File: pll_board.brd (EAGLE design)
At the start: 50 x 50 mm, 86 parts, among them U1 SI5351C, U3 MCP47X6, U4 LD117AS33TR, U5 74AC74D, X0 SMA-142-0711-871/876, X1 SMA-142-0711-871/876, X2 SMA-142-0711-871/876, X3 SMA-142-0711-871/876, X4 SMA-142-0711-871/876, X5 SMA-142-0711-871/876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

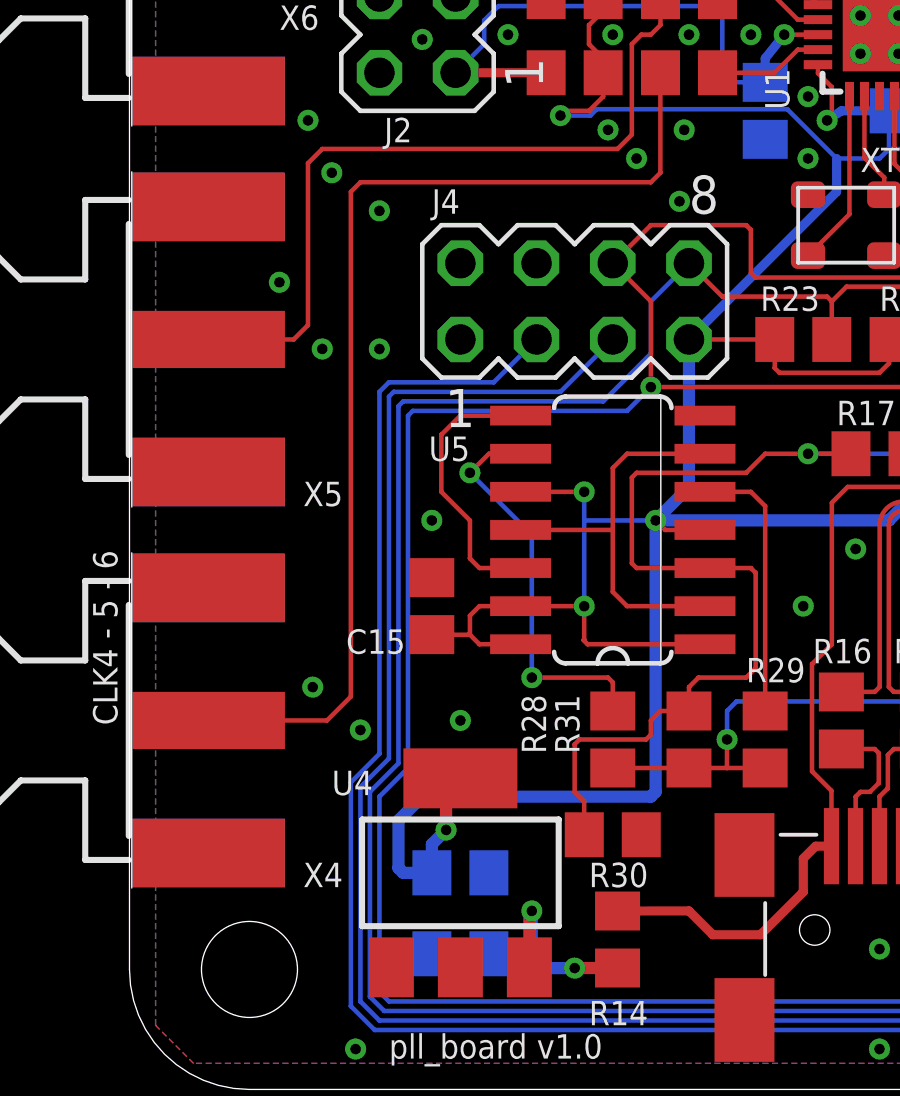
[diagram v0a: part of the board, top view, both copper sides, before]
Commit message: Add USB +5V on i2c/uart connector.
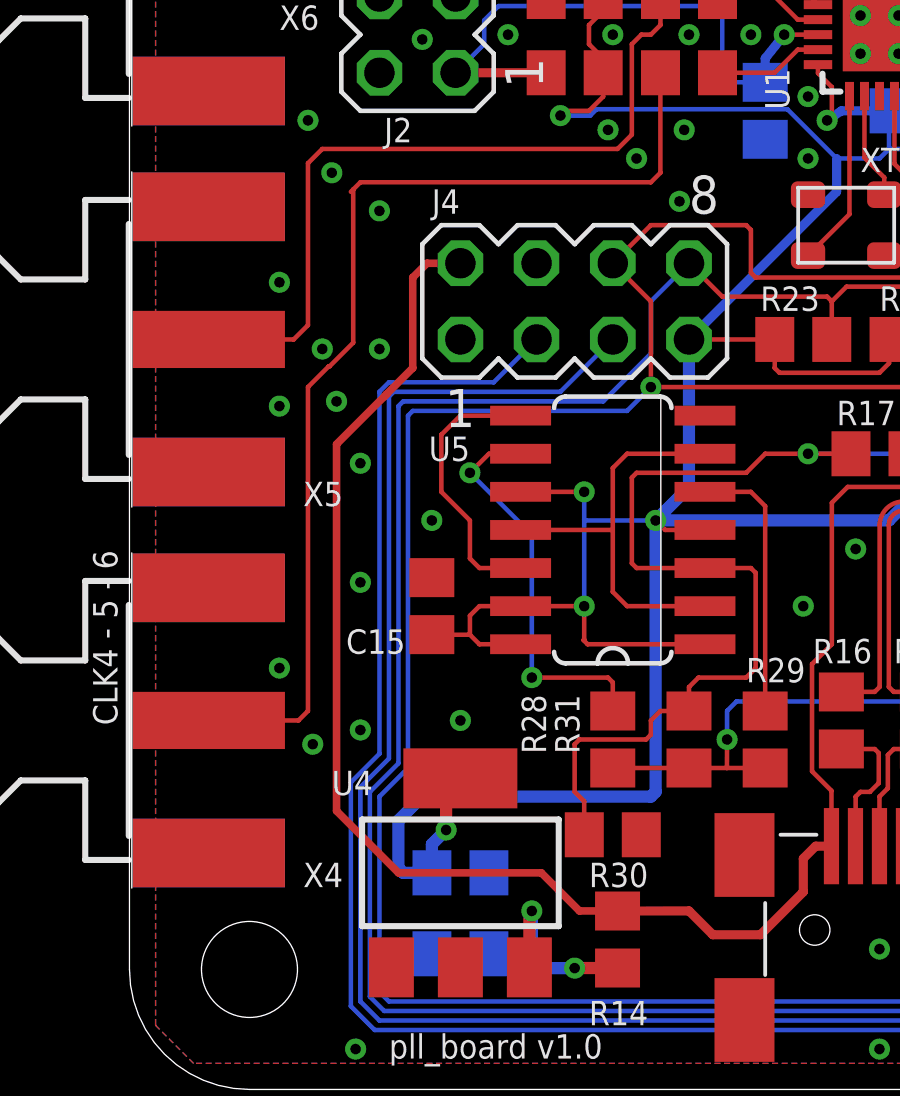
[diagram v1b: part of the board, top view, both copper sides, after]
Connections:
- net +5V: now also J4.2
- net GND: now also J4.4
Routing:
- net +5V: track 33.9 -> 65.4 mm
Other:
- board text added: "Si5351C PLL + ATmega32U4 PLL / OCXO-Control / Clock Generator V1.1 <vogelchr@vogel.cx> http://github.com/vogelchr/pll_board/"
- board text removed: "Si5351C PLL + ATmega32U4 PLL / OCXO-Control / Clock Generator V1.0 <vogelchr@vogel.cx> http://github.com/vogelchr/pll_board/"
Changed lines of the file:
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@@
 <text x="37.94125" y="9.04875" size="0.8128" layer="26" font="vector" rot="MR0">Si5351C PLL + ATmega32U4
 PLL / OCXO-Control / Clock Generator
-V1.0 &lt;vogelchr@vogel.cx&gt;
+V1.1 &lt;vogelchr@vogel.cx&gt;
 http://github.com/vogelchr/pll_board/</text>
 <text x="10.31875" y="2.69875" size="0.8128" layer="25" font="vector">pll_board v1.0</text>
@@
 <via x="17.78" y="36.83" extent="1-16" drill="0.35"/>
 <via x="8.41375" y="32.22625" extent="1-16" drill="0.35"/>
-<via x="7.77875" y="15.08125" extent="1-16" drill="0.35"/>
-<via x="9.36625" y="13.6525" extent="1-16" drill="0.35"/>
+<via x="6.6675" y="15.71625" extent="1-16" drill="0.35"/>
+<via x="7.77875" y="13.17625" extent="1-16" drill="0.35"/>
 <via x="8.09625" y="26.3525" extent="1-16" drill="0.35"/>
 <via x="6.6675" y="28.575" extent="1-16" drill="0.35"/>
@@
 <via x="36.5125" y="23.01875" extent="1-16" drill="0.35"/>
 <via x="28.575" y="20.32" extent="1-16" drill="0.35"/>
+<contactref element="J4" pad="4"/>
+<via x="9.36625" y="13.6525" extent="1-16" drill="0.35"/>
+<via x="9.36625" y="18.57375" extent="1-16" drill="0.35"/>
+<via x="9.36625" y="22.5425" extent="1-16" drill="0.35"/>
 <wire x1="26.035" y1="36.195" x2="26.67" y2="36.83" width="0" layer="19" extent="1-1"/>
+<via x="8.5725" y="24.60625" extent="1-16" drill="0.35"/>
+<via x="6.6675" y="24.4475" extent="1-16" drill="0.35"/>
 </signal>
 <signal name="CLK0_SMA">
@@
 <contactref element="R5" pad="2"/>
 <contactref element="X4" pad="1"/>
-<wire x1="4.31165" y1="13.97" x2="8.255" y2="13.97" width="0.1524" layer="1"/>
-<wire x1="8.255" y1="13.97" x2="9.04875" y2="14.76375" width="0.1524" layer="1"/>
-<wire x1="9.04875" y1="14.76375" x2="9.04875" y2="31.59125" width="0.1524" layer="1"/>
-<wire x1="9.04875" y1="31.59125" x2="9.36625" y2="31.90875" width="0.1524" layer="1"/>
+<wire x1="9.04875" y1="31.59125" x2="9.128125" y2="31.670625" width="0.1524" layer="1"/>
+<wire x1="9.128125" y1="31.670625" x2="9.36625" y2="31.90875" width="0.1524" layer="1"/>
 <wire x1="19.05" y1="31.90875" x2="19.3675" y2="32.22625" width="0.1524" layer="1"/>
 <wire x1="19.3675" y1="32.22625" x2="19.3675" y2="35.5575" width="0.1524" layer="1"/>
 <wire x1="19.3675" y1="35.5575" x2="19.37" y2="35.56" width="0.1524" layer="1"/>
 <wire x1="9.36625" y1="31.90875" x2="19.05" y2="31.90875" width="0.1524" layer="1"/>
+<wire x1="8.337075" y1="25.7711" x2="8.3086" y2="25.7711" width="0.1524" layer="1"/>
+<wire x1="8.3086" y1="25.7711" x2="7.62" y2="25.0825" width="0.1524" layer="1"/>
+<wire x1="9.128125" y1="31.670625" x2="9.128125" y2="26.56215" width="0.1524" layer="1"/>
+<wire x1="9.128125" y1="26.56215" x2="8.337075" y2="25.7711" width="0.1524" layer="1"/>
+<wire x1="7.62" y1="25.0825" x2="7.62" y2="14.2875" width="0.1524" layer="1"/>
+<wire x1="7.62" y1="14.2875" x2="7.3025" y2="13.97" width="0.1524" layer="1"/>
+<wire x1="7.3025" y1="13.97" x2="4.31165" y2="13.97" width="0.1524" layer="1"/>
 </signal>
 <signal name="CLK5_SMA">
@@
 <wire x1="22.70125" y1="6.82625" x2="21.11375" y2="6.82625" width="0.3048" layer="1"/>
 <wire x1="21.11375" y1="6.82625" x2="20.32" y2="7.62" width="0.3048" layer="1"/>
-<wire x1="20.32" y1="7.62" x2="17.93875" y2="7.6175" width="0.3048" layer="1"/>
+<wire x1="17.93875" y1="7.6175" x2="20.32" y2="7.62" width="0.3048" layer="1"/>
 <wire x1="31.03" y1="22.25" x2="32.0425" y2="22.25" width="0.1524" layer="1"/>
 <wire x1="32.0425" y1="22.25" x2="32.22625" y2="22.06625" width="0.1524" layer="1"/>
@@
 <wire x1="24.4214" y1="12.2753125" x2="24.4214" y2="15.8489" width="0.1524" layer="1"/>
 <wire x1="25.60999375" y1="21.7548" x2="28.7398" y2="21.7548" width="0.1524" layer="1"/>
+<contactref element="J4" pad="2"/>
+<wire x1="12.7" y1="29.21" x2="11.58875" y2="29.21" width="0.254" layer="1"/>
+<wire x1="11.58875" y1="29.21" x2="11.1125" y2="28.73375" width="0.254" layer="1"/>
+<wire x1="11.1125" y1="25.7175" x2="11.1125" y2="28.73375" width="0.254" layer="1"/>
+<wire x1="10.63625" y1="8.89" x2="15.39875" y2="8.89" width="0.254" layer="1"/>
+<wire x1="15.39875" y1="8.89" x2="16.66875" y2="7.62" width="0.254" layer="1"/>
+<wire x1="16.66875" y1="7.62" x2="17.93625" y2="7.62" width="0.254" layer="1"/>
+<wire x1="17.93625" y1="7.62" x2="17.93875" y2="7.6175" width="0.254" layer="1"/>
+<wire x1="10.16" y1="24.765" x2="10.239375" y2="24.844375" width="0.254" layer="1"/>
+<wire x1="10.239375" y1="24.844375" x2="11.1125" y2="25.7175" width="0.254" layer="1"/>
+<wire x1="10.239375" y1="24.844375" x2="8.5725" y2="23.1775" width="0.254" layer="1"/>
+<wire x1="8.5725" y1="23.1775" x2="8.5725" y2="10.95375" width="0.254" layer="1"/>
+<wire x1="8.5725" y1="10.95375" x2="10.63625" y2="8.89" width="0.254" layer="1"/>
 </signal>
 <signal name="N$11">
